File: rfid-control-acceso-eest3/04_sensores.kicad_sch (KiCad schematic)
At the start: 17 parts, among them J10 DSC_LC100_TAMPER_NC, J6 REED_NC, J7 DSC_LC100_PWR_ALARM_NC, J8 CABINET_SENSOR

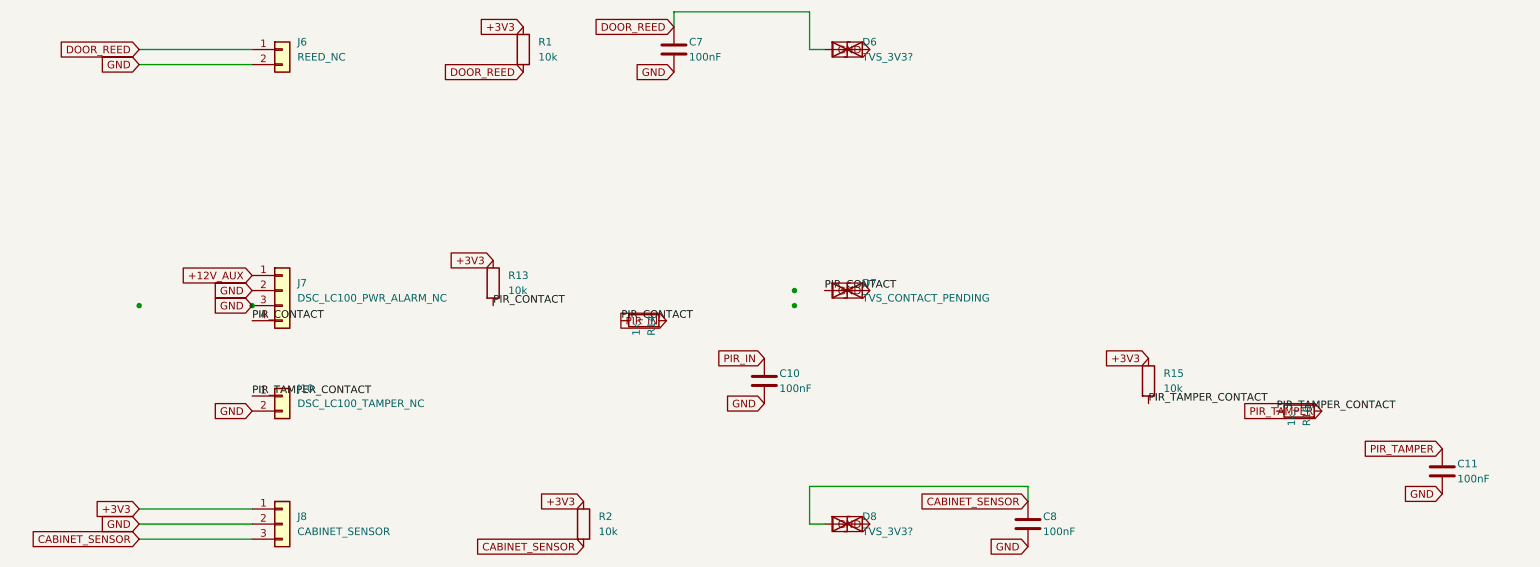
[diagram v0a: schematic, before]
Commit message: Reorganiza floorplan PCB Rev A antes del ruteo
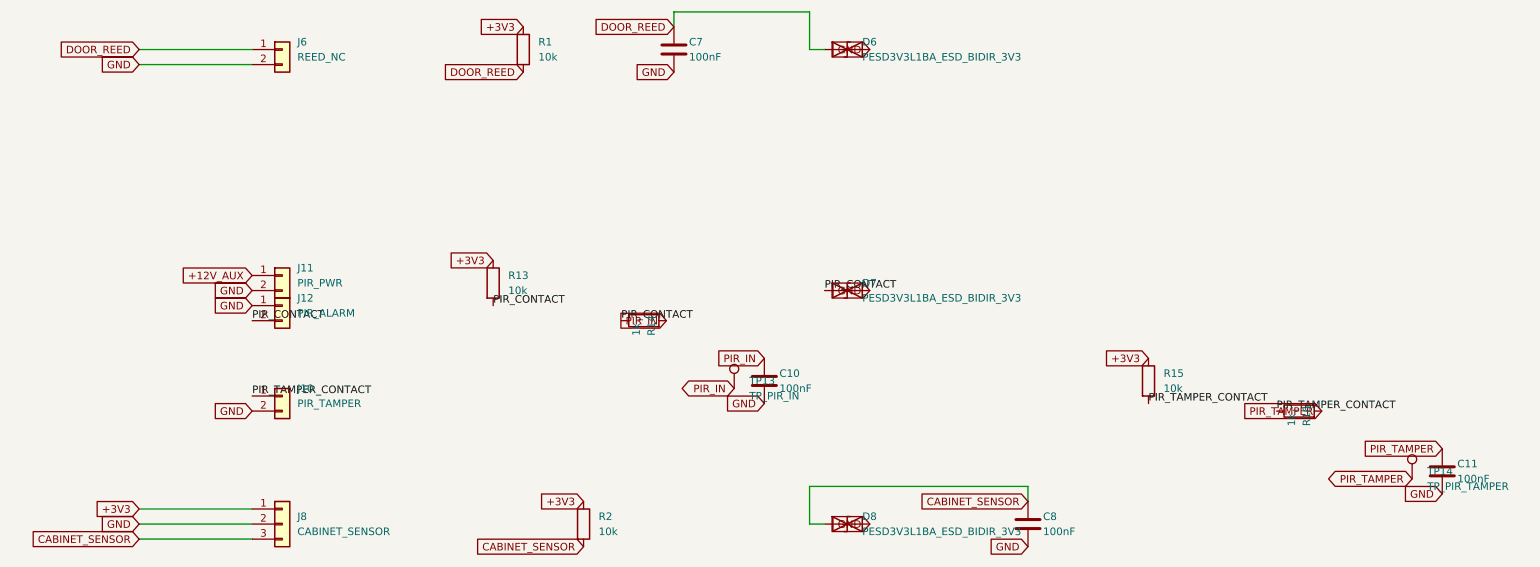
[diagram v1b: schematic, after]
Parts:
- removed J7: DSC_LC100_PWR_ALARM_NC, symbol Connector_Generic:Conn_01x04
- added J11: PIR_PWR, rfid_eest3:KF301_2P_P5.08_PLACEHOLDER_NO_FABRICAR, symbol Connector_Generic:Conn_01x02
- added J12: PIR_ALARM, rfid_eest3:KF301_2P_P5.08_PLACEHOLDER_NO_FABRICAR, symbol Connector_Generic:Conn_01x02
- added TP13: TP_PIR_IN, TestPoint:TestPoint_THTPad_D2.0mm_Drill1.0mm, symbol Connector:TestPoint
- added TP14: TP_PIR_TAMPER, TestPoint:TestPoint_THTPad_D2.0mm_Drill1.0mm, symbol Connector:TestPoint
- C10, C11, C7, C8: footprint (none) -> Capacitor_THT:C_Disc_D5.0mm_W2.5mm_P5.00mm
- D6, D8: value TVS_3V3? -> PESD3V3L1BA_ESD_BIDIR_3V3; footprint (none) -> Diode_SMD:D_SOD-323; MPN (none) -> PESD3V3L1BA,115; Manufacturer (none) -> Nexperia
- D7: value TVS_CONTACT_PENDING -> PESD3V3L1BA_ESD_BIDIR_3V3; footprint (none) -> Diode_SMD:D_SOD-323; MPN (none) -> PESD3V3L1BA,115; Manufacturer (none) -> Nexperia
- J10: value DSC_LC100_TAMPER_NC -> PIR_TAMPER; footprint (none) -> rfid_eest3:KF301_2P_P5.08_PLACEHOLDER_NO_FABRICAR; Terminal_Names (none) -> 1=T1; 2=T2
- J6: footprint (none) -> rfid_eest3:KF301_2P_P5.08_PLACEHOLDER_NO_FABRICAR
- J8: footprint (none) -> rfid_eest3:KF301_3P_P5.08_PLACEHOLDER_NO_FABRICAR
- R1, R13, R14, R15, R16, R2: footprint (none) -> Resistor_THT:R_Axial_DIN0207_L6.3mm_D2.5mm_P10.16mm_Horizontal
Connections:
- net +12V_AUX: now also J11.1 (Pin_1)
- net GND: now also J11.2 (Pin_2), J12.1 (Pin_1)
- net PIR_CONTACT: now also J12.2 (Pin_2)
- net PIR_IN: now also TP13.1
- net PIR_TAMPER: now also TP14.1
